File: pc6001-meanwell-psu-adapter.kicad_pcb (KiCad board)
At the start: 2 copper layers, 224 x 84 mm, 3 parts

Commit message: Power entry connector
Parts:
- added REF**: Qualitek_770W-X2-13_IEC_C8, PowerEntry:Qualitek_770W-X2-13_IEC_C8, F.Cu at (273.9, 111.4)
- added REF**: MountingHole_3.2mm_M3, MountingHole:MountingHole_3.2mm_M3, F.Cu at (264.2, 91.6)
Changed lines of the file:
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@@
   )
   (net 0 "")
+  (footprint "PowerEntry:Qualitek_770W-X2-13_IEC_C8" (layer "F.Cu")
+    (at 273.95 111.4 90)
+    (fp_text reference "REF**" (at 0 -0.5 90 unlocked) (layer "F.SilkS") hide
+        (effects (font (size 1 1) (thickness 0.1)))
+    )
+    (fp_text value "Qualitek_770W-X2-13_IEC_C8" (at 0 1 90 unlocked) (layer "F.Fab")
+        (effects (font (size 1 1) (thickness 0.15)))
+    )
+    (fp_text user "${REFERENCE}" (at 0 2.5 90 unlocked) (layer "F.Fab")
+        (effects (font (size 1 1) (thickness 0.15)))
+    )
+    (fp_rect (start -12.8 -17.9) (end 15.8 -1.6)
+      (stroke (width 0.1) (type default)) (fill none) (layer "F.SilkS"))
+    (fp_line (start -10.8 -13.6) (end -10.8 -6)
+      (stroke (width 0.05) (type default)) (layer "Edge.Cuts"))
+    (fp_line (start -10.8 -6) (end -8.3 -6)
+      (stroke (width 0.05) (type default)) (layer "Edge.Cuts"))
+    (fp_line (start -8.3 -16.1) (end -8.3 -13.6)
+      (stroke (width 0.05) (type default)) (layer "Edge.Cuts"))
+    (fp_line (start -8.3 -13.6) (end -10.8 -13.6)
+      (stroke (width 0.05) (type default)) (layer "Edge.Cuts"))
+    (fp_line (start -8.3 -6) (end -8.3 -3.5)
+      (stroke (width 0.05) (type default)) (layer "Edge.Cuts"))
+    (fp_line (start -8.3 -3.5) (end 11.3 -3.5)
+      (stroke (width 0.05) (type default)) (layer "Edge.Cuts"))
+    (fp_line (start 11.3 -16.1) (end -8.3 -16.1)
+      (stroke (width 0.05) (type default)) (layer "Edge.Cuts"))
+    (fp_line (start 11.3 -13.6) (end 11.3 -16.1)
+      (stroke (width 0.05) (type default)) (layer "Edge.Cuts"))
+    (fp_line (start 11.3 -6) (end 13.8 -6)
+      (stroke (width 0.05) (type default)) (layer "Edge.Cuts"))
+    (fp_line (start 11.3 -3.5) (end 11.3 -6)
+      (stroke (width 0.05) (type default)) (layer "Edge.Cuts"))
+    (fp_line (start 13.8 -13.6) (end 11.3 -13.6)
+      (stroke (width 0.05) (type default)) (layer "Edge.Cuts"))
+    (fp_line (start 13.8 -6) (end 13.8 -13.6)
+      (stroke (width 0.05) (type default)) (layer "Edge.Cuts"))
+  )
   (footprint "Panelization.pretty-master:mouse-bite-5mm-slot" (layer "F.Cu")
     (at 249.5 125.75 90)
@@
     (pad "" np_thru_hole circle (at 3.75 2.5 90) (size 0.5 0.5) (drill 0.5) (layers "*.Cu" "*.Mask"))
   )
+  (footprint "MountingHole:MountingHole_3.2mm_M3" (layer "F.Cu")
+    (at 264.2 91.6)
+    (descr "Mounting Hole 3.2mm, no annular, M3")
+    (tags "mounting hole 3.2mm no annular m3")
+    (attr exclude_from_pos_files exclude_from_bom)
+    (fp_text reference "REF**" (at 0 -4.2) (layer "F.SilkS") hide
+        (effects (font (size 1 1) (thickness 0.15)))
+    )
+    (fp_text value "MountingHole_3.2mm_M3" (at 0 4.2) (layer "F.Fab")
+        (effects (font (size 1 1) (thickness 0.15)))
+    )
+    (fp_text user "${REFERENCE}" (at 0 0) (layer "F.Fab")
+        (effects (font (size 1 1) (thickness 0.15)))
+    )
+    (fp_circle (center 0 0) (end 3.2 0)
+      (stroke (width 0.15) (type solid)) (fill none) (layer "Cmts.User"))
+    (fp_circle (center 0 0) (end 3.45 0)
+      (stroke (width 0.05) (type solid)) (fill none) (layer "F.CrtYd"))
+    (pad "" np_thru_hole circle (at 0 0) (size 3.2 3.2) (drill 3.2) (layers "*.Cu" "*.Mask"))
+  )
   (footprint "Panelization.pretty-master:mouse-bite-5mm-slot" (layer "F.Cu")

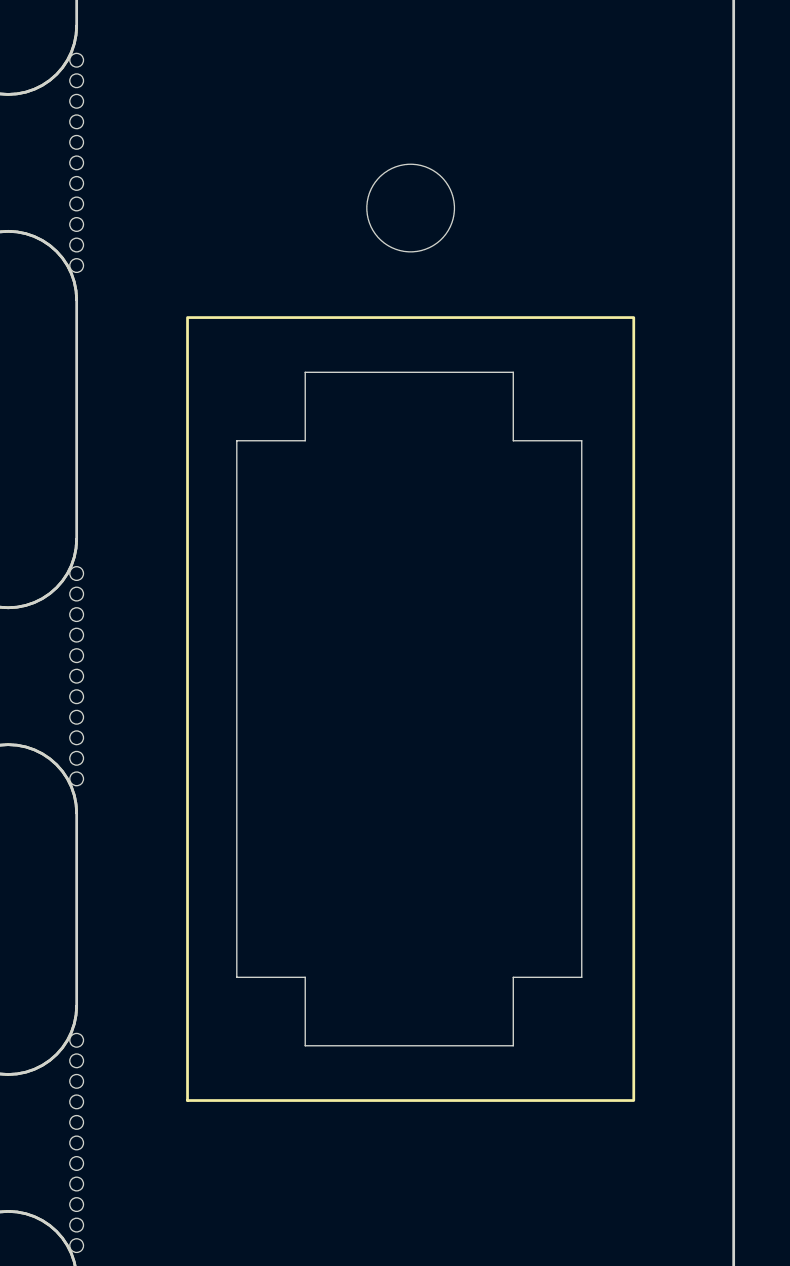
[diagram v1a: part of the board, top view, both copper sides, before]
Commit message: Move the dummy plug up just a little bit more
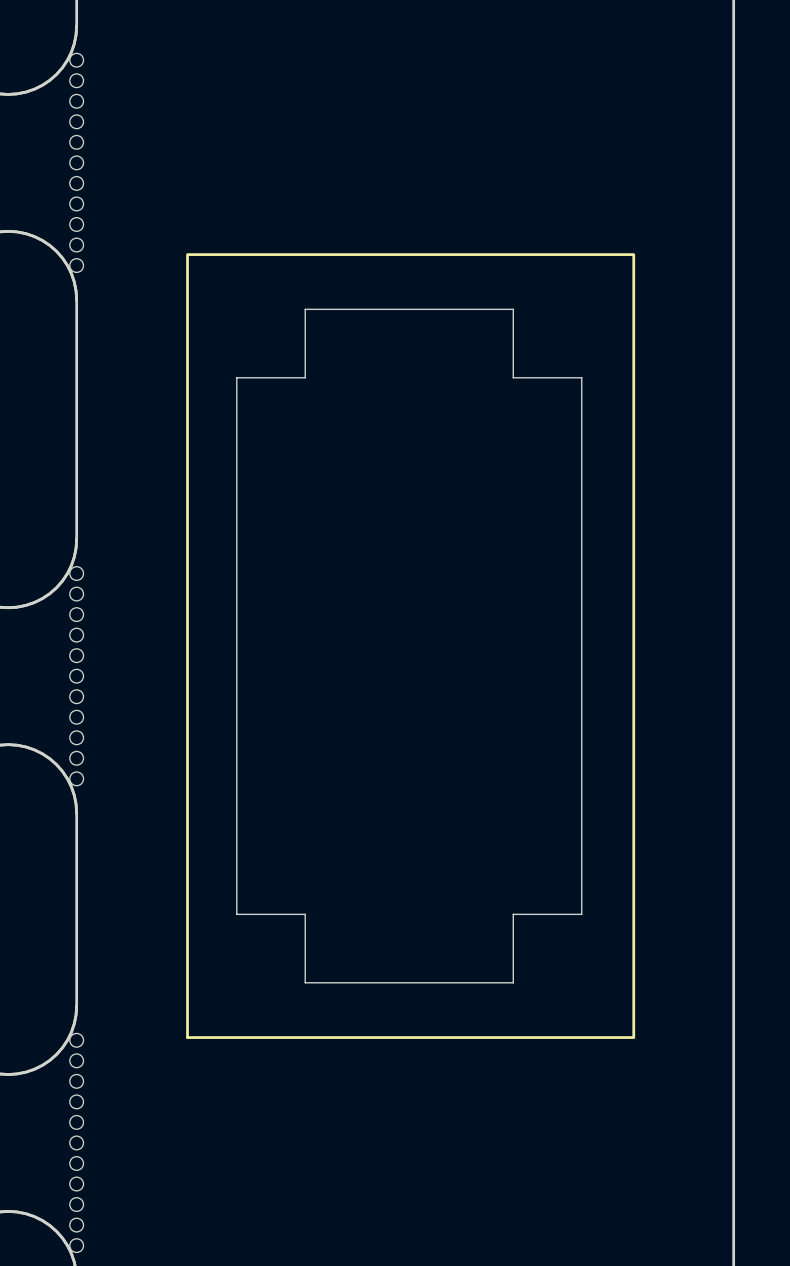
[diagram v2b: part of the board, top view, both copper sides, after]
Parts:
- removed the REF** at (264.2, 91.6)
- moved REF** 2.30 mm to (273.9, 109.1)
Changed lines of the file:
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@@
   (net 0 "")
   (footprint "PowerEntry:Qualitek_770W-X2-13_IEC_C8" (layer "F.Cu")
-    (at 273.95 111.4 90)
+    (at 273.95 109.1 90)
     (fp_text reference "REF**" (at 0 -0.5 90 unlocked) (layer "F.SilkS") hide
         (effects (font (size 1 1) (thickness 0.1)))
@@
     (pad "" np_thru_hole circle (at 3.75 2.5 90) (size 0.5 0.5) (drill 0.5) (layers "*.Cu" "*.Mask"))
   )
-  (footprint "MountingHole:MountingHole_3.2mm_M3" (layer "F.Cu")
-    (at 264.2 91.6)
-    (descr "Mounting Hole 3.2mm, no annular, M3")
-    (tags "mounting hole 3.2mm no annular m3")
-    (attr exclude_from_pos_files exclude_from_bom)
-    (fp_text reference "REF**" (at 0 -4.2) (layer "F.SilkS") hide
-        (effects (font (size 1 1) (thickness 0.15)))
-    )
-    (fp_text value "MountingHole_3.2mm_M3" (at 0 4.2) (layer "F.Fab")
-        (effects (font (size 1 1) (thickness 0.15)))
-    )
-    (fp_text user "${REFERENCE}" (at 0 0) (layer "F.Fab")
-        (effects (font (size 1 1) (thickness 0.15)))
-    )
-    (fp_circle (center 0 0) (end 3.2 0)
-      (stroke (width 0.15) (type solid)) (fill none) (layer "Cmts.User"))
-    (fp_circle (center 0 0) (end 3.45 0)
-      (stroke (width 0.05) (type solid)) (fill none) (layer "F.CrtYd"))
-    (pad "" np_thru_hole circle (at 0 0) (size 3.2 3.2) (drill 3.2) (layers "*.Cu" "*.Mask"))
-  )
   (footprint "Panelization.pretty-master:mouse-bite-5mm-slot" (layer "F.Cu")

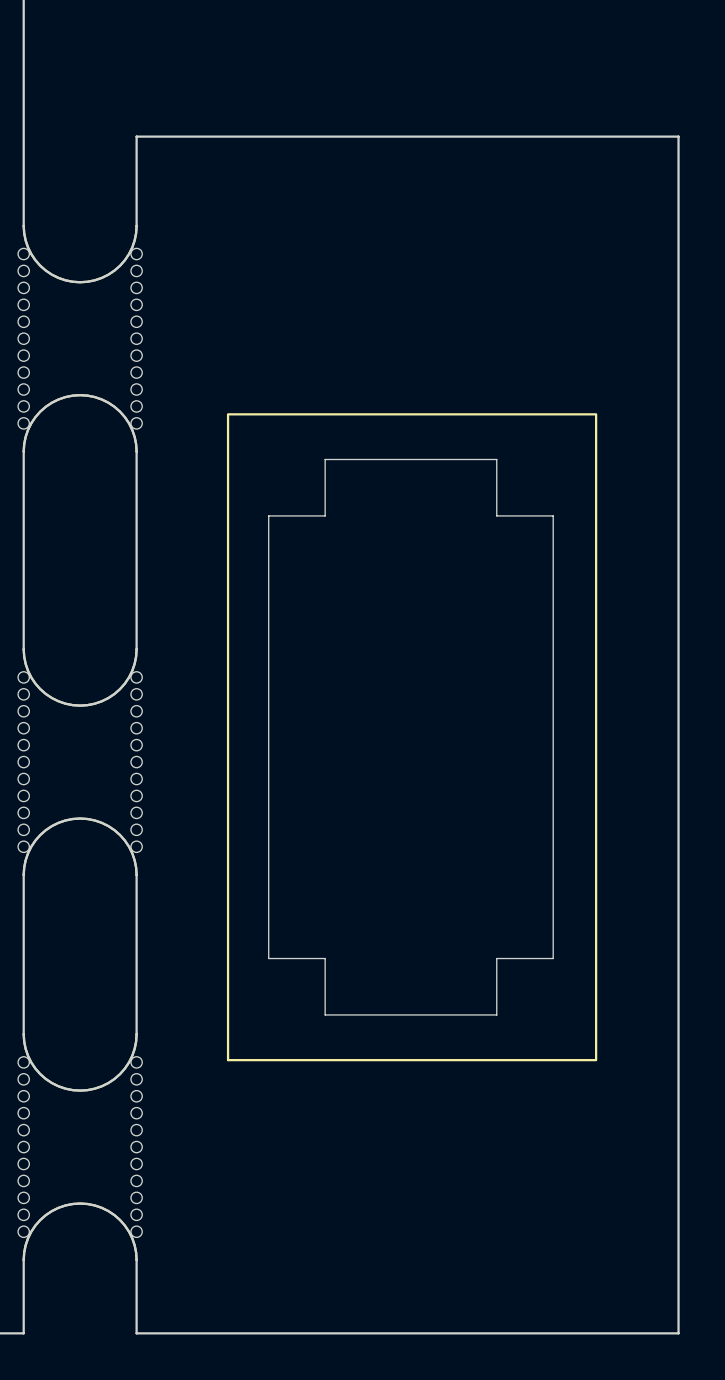
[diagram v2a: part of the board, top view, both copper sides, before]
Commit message: Better horizontal misalignment tolerance
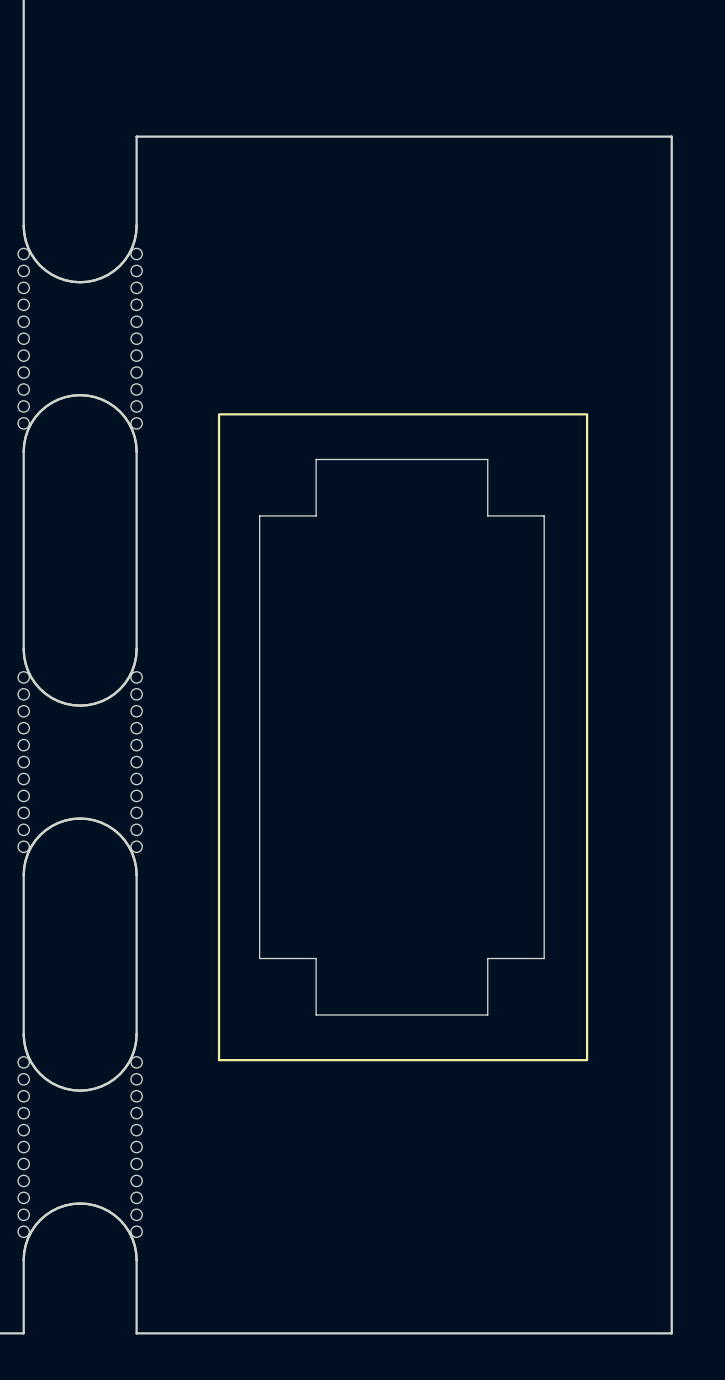
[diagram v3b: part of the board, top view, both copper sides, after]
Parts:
- moved REF** 0.40 mm to (273.6, 109.1)
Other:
- board size 224 x 84 mm -> 223.7 x 84 mm
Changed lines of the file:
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@@
   (net 0 "")
   (footprint "PowerEntry:Qualitek_770W-X2-13_IEC_C8" (layer "F.Cu")
-    (at 273.95 109.1 90)
+    (at 273.55 109.1 90)
     (fp_text reference "REF**" (at 0 -0.5 90 unlocked) (layer "F.SilkS") hide
         (effects (font (size 1 1) (thickness 0.1)))
@@
     (pad "" np_thru_hole circle (at 3.75 2.5 90) (size 0.5 0.5) (drill 0.5) (layers "*.Cu" "*.Mask"))
   )
+  (gr_line (start 252 81) (end 275.7 81)
+    (stroke (width 0.1) (type default)) (layer "Edge.Cuts"))
   (gr_line (start 52 134) (end 247 134)
     (stroke (width 0.1) (type default)) (layer "Edge.Cuts"))
@@
   (gr_line (start 252 134) (end 252 130.75)
     (stroke (width 0.1) (type default)) (layer "Edge.Cuts"))
-  (gr_line (start 252 134) (end 276 134)
-    (stroke (width 0.1) (type default)) (layer "Edge.Cuts"))
   (gr_line (start 252 84.95) (end 252 81)
     (stroke (width 0.1) (type default)) (layer "Edge.Cuts"))
@@
   (gr_line (start 52 134) (end 52 50)
     (stroke (width 0.1) (type default)) (layer "Edge.Cuts"))
-  (gr_line (start 276 134) (end 276 81)
+  (gr_line (start 275.7 134) (end 275.7 81)
     (stroke (width 0.1) (type default)) (layer "Edge.Cuts"))
   (gr_line (start 252 120.75) (end 252 113.7)
@@
   (gr_line (start 247 84.95) (end 247 60)
     (stroke (width 0.1) (type default)) (layer "Edge.Cuts"))
+  (gr_line (start 275.7 134) (end 252 134)
+    (stroke (width 0.1) (type default)) (layer "Edge.Cuts"))
   (gr_line (start 237 50) (end 247 60)
     (stroke (width 0.1) (type default)) (layer "Edge.Cuts"))
-  (gr_line (start 276 81) (end 252 81)
-    (stroke (width 0.1) (type default)) (layer "Edge.Cuts"))
   (gr_text "TODO: make smaller if possible" (at 137 130) (layer "Cmts.User")
